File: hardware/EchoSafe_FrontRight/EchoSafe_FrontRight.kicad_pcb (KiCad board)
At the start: 2 copper layers, 54 x 40 mm, 5 parts, among them J1 Conn_Harness_09, M1 C0720B001F

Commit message: Add acoustic port holes to mic modules, fix mic footprint pad positions
Adding the acoustic port hole (ICS-43434 datasheet: >=0.5mm diameter,
centered under the GND ring) exposed that the mic footprint's pad
positions -- authored earlier this session -- didn't match the real
chip at all: a simple 2x2-corner grid instead of the datasheet's actual
3-pad/2-pad row layout. Re-derived the correct pad positions from the
datasheet's mechanical package drawing (DS-000069 Rev 1.2, Figure 15)
via pixel-level measurement rather than reading dimension lines by eye,
cross-checked against reconstructed package width and the PIN#1
reference corner marker.

Also rebuilt the GND pad as a true annulus (was a solid disc) so the
hole has real clearance, shaved its OD from the datasheet's 1.625mm to
1.1mm to resolve a genuine overlap with the now-correctly-positioned
SCK/LR pads (real chip-scale pitch, not a mistake), and added a scoped
per-project DRC rule for the resulting sub-0.2mm chip-internal spacing
that the board's generic netclass rule doesn't accommodate.

Re-routed all 4 module boards from scratch after the pad reposition.
Verified via kicad-cli pcb drc: 0 violations, 0 unconnected pads on
every board. Still not a physical measurement -- flagged in CLAUDE.md
for verification against real hardware before fabrication.

Co-Authored-By: Claude Sonnet 5 <noreply@anthropic.com>
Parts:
- added H1: Acoustic_Port_0.5mm, Acoustic_Port_0.5mm, F.Cu at (32.0, 8.00)
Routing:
- net GND: track 77.0 -> 32.0 mm, vias 4 -> 2
- net MOTOR_TR_OUTP: track 29.6 -> 19.7 mm, vias 2 -> 0
- net MOTOR_TR_OUTN: track 27.4 -> 18.9 mm, vias 2 -> 0
- net SPK_OUTN: track 33.2 -> 27.9 mm
- net 3V3_SYS: track 36.1 -> 31.1 mm, vias 4 -> 2
- net MIC_TOP_SCK: track 29.9 -> 25.8 mm
- net SPK_OUTP: track 33.0 -> 30.4 mm
- net MIC_TOP_SD: track 27.8 -> 30.4 mm
- net MIC_TOP_WS: track 31.1 -> 28.9 mm

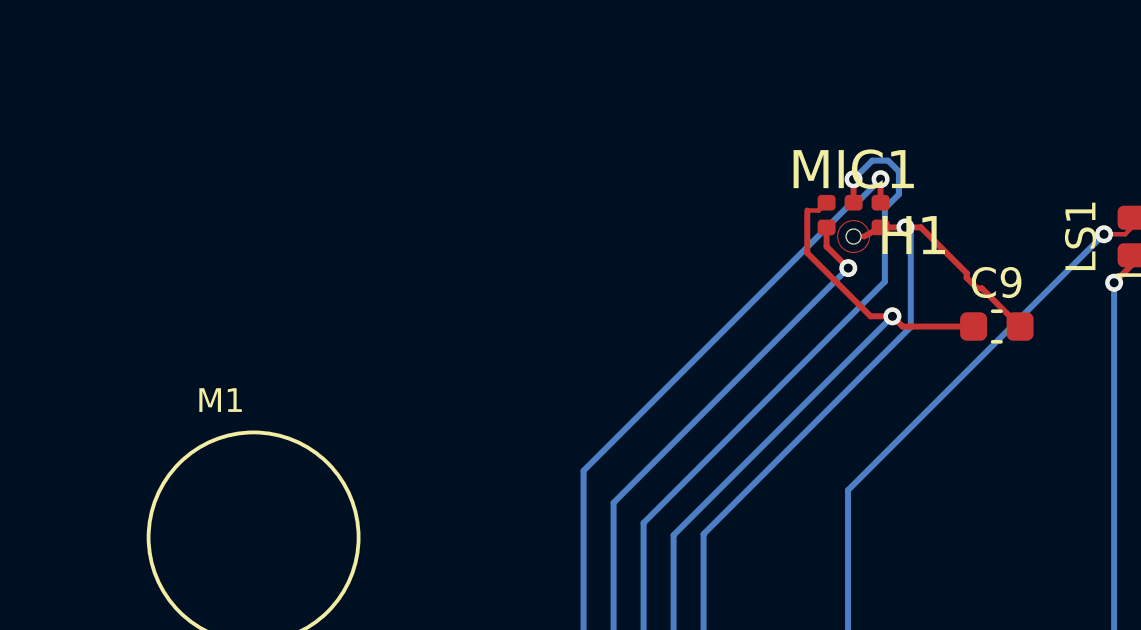
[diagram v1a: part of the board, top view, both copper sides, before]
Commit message: Visual/silkscreen review: fix footprint FPID prefixes and silkscreen overlaps
kicad-cli pcb drc was only ever run at default severity, which silently
excludes the silk_over_copper/silk_overlap/text_height checks. Re-running
with --severity-all, plus rendering true F.SilkS-only SVGs (previous
renders mixed in F.Fab assembly-doc text, making boards look far more
cluttered than they are), surfaced real issues:

- Every placed footprint on all 5 boards had lost its library prefix
  (bare name, no "Library:" qualifier) despite correct fp-lib-table
  registrations -- pcbnew's Python API doesn't preserve FPID library
  nicknames across a FootprintLoad()/board.Add() round-trip unless
  SetFPID() is called explicitly. Fixed across all 5 boards.
- The custom TP4056_Module footprint had its pads listing F.SilkS in
  their own layer set (guaranteed self-violation on every pad) and
  center-justified pin labels straddling the outline/pad edges. Fixed
  in the library footprint and re-synced onto the central pod.
- H1 (acoustic port) and M1 (motor) reference text overlapped MIC1's
  pads and undersized text vs. the board's minimum, respectively --
  fixed in their library footprints and re-synced onto all 4 modules.
- U2's reference sat on its own QFN thermal pad; C8's reference
  overlapped neighboring C4's silkscreen; U1/U2 each carried a literal
  duplicate coincident silkscreen text object (UltraLibrarian import
  artifact). All fixed.

All 5 boards now show 0 DRC violations at full severity (previously
only verified at default severity). Two items flagged but left
unfixed since they'd require hand-editing KiCad's own shared global
library footprints: J1/LS1 connectors have no pin-1 marker on the
physically-printed silkscreen (only on F.Fab), and U1's reference
will be hidden under the soldered ESP32 module.

Co-Authored-By: Claude Sonnet 5 <noreply@anthropic.com>
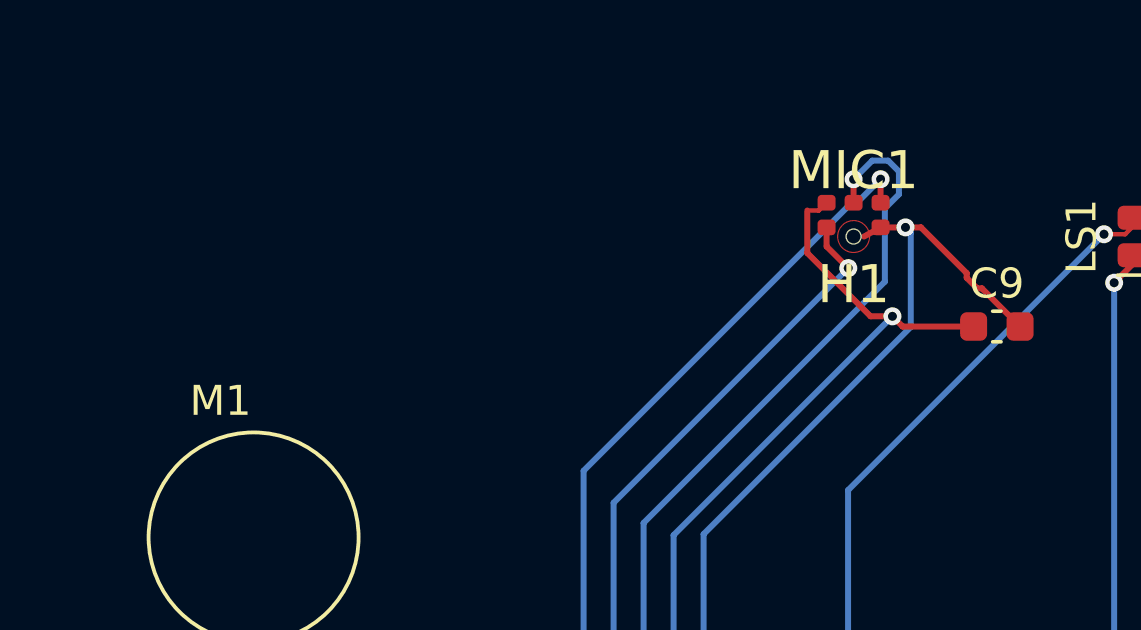
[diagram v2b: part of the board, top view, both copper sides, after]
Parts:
- C9: footprint C_0603_1608Metric -> Capacitor_SMD:C_0603_1608Metric
- H1: footprint Acoustic_Port_0.5mm -> ICS-43434:Acoustic_Port_0.5mm
- J1: footprint JST_SH_SM09B-SRSS-TB_1x09-1MP_P1.00mm_Horizontal -> Connector_JST:JST_SH_SM09B-SRSS-TB_1x09-1MP_P1.00mm_Horizontal
- LS1: footprint Molex_PicoBlade_53261-0271_1x02-1MP_P1.25mm_Horizontal -> Connector_Molex:Molex_PicoBlade_53261-0271_1x02-1MP_P1.25mm_Horizontal
- M1: value C0720B001F -> XDCR_C0720B001F; footprint XDCR_C0720B001F -> C0720B001F:XDCR_C0720B001F
- MIC1: footprint ICS-43434_LGA6 -> ICS-43434:ICS-43434_LGA6

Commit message: Add pin-1 silkscreen markers and relocate U1's hidden reference
Follow-up to the visual/silkscreen review: both previously-flagged
items are now addressed.

- J1 (all 4 modules + central pod J2-J5) and LS1 (front modules) used
  KiCad's stock Connector_JST/Connector_Molex footprints, whose F.SilkS
  pin-1 indicator is only a subtle asymmetric notch in the outline
  (easy to miss at this scale) -- not, as first described, entirely
  absent. Rather than hand-edit KiCad's shared global libraries, added
  a project-local override library (lib/symbols/Connectors_PinMarked.pretty)
  with a bold pin-1 dot added to each of the 3 affected footprints, and
  resynced every affected instance onto it.
- U1 (ESP32-S3-WROOM-1)'s reference sat inside the module's own
  footprint outline (hidden once the module is soldered down).
  Checked every neighboring footprint and routed trace via pcbnew's
  Python API to see if it could move outside the outline into open
  board area -- it can't; this board was deliberately packed to a
  minimum practical 65x90mm and nothing borders U1 with room to spare.
  Moved the reference within the footprint's own interior instead, to
  a pocket clear of the trace and secondary pad cluster it previously
  sat on top of -- fully legible pre-assembly, same as before post-
  assembly (matches the original "cosmetic only" assessment).

All 5 boards re-verified at 0 DRC violations, full severity.

Co-Authored-By: Claude Sonnet 5 <noreply@anthropic.com>
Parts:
- J1: value Conn_Harness_09 -> JST_SH_SM09B-SRSS-TB_1x09-1MP_P1.00mm_Horizontal; footprint Connector_JST:JST_SH_SM09B-SRSS-TB_1x09-1MP_P1.00mm_Horizontal -> Connectors_PinMarked:JST_SH_SM09B-SRSS-TB_1x09-1MP_P1.00mm_Horizontal
- LS1: value Adafruit_4227_8ohm_1W -> Molex_PicoBlade_53261-0271_1x02-1MP_P1.25mm_Horizontal; footprint Connector_Molex:Molex_PicoBlade_53261-0271_1x02-1MP_P1.25mm_Horizontal -> Connectors_PinMarked:Molex_PicoBlade_53261-0271_1x02-1MP_P1.25mm_Horizontal
